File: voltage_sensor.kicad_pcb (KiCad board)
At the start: 2 copper layers, 41.6 x 56.6 mm, 24 parts, among them K1 REF, P1 Input, P2 CONN_4, P3 CONN_2, U1 REF5020, U2 LT6011, U3 ADUM5401, U4 MCP3550

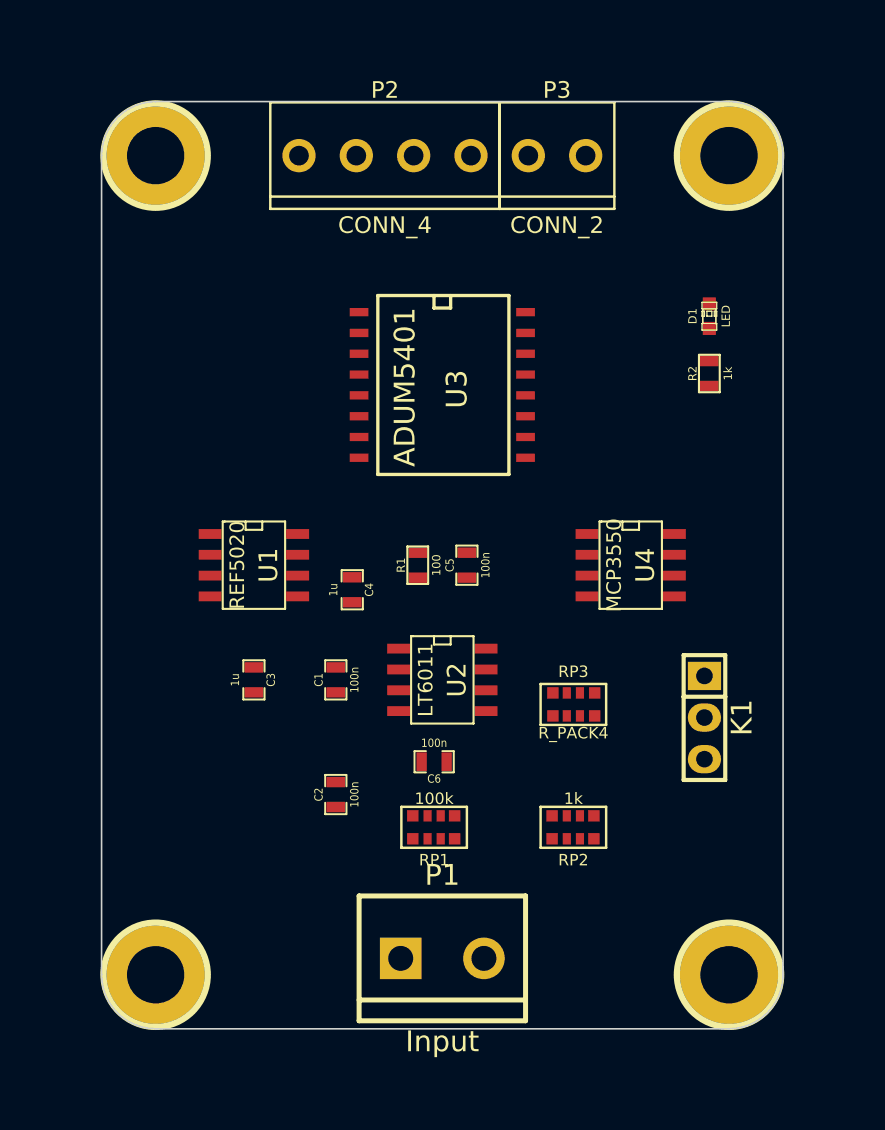
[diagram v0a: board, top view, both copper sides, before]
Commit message: Added filter caps
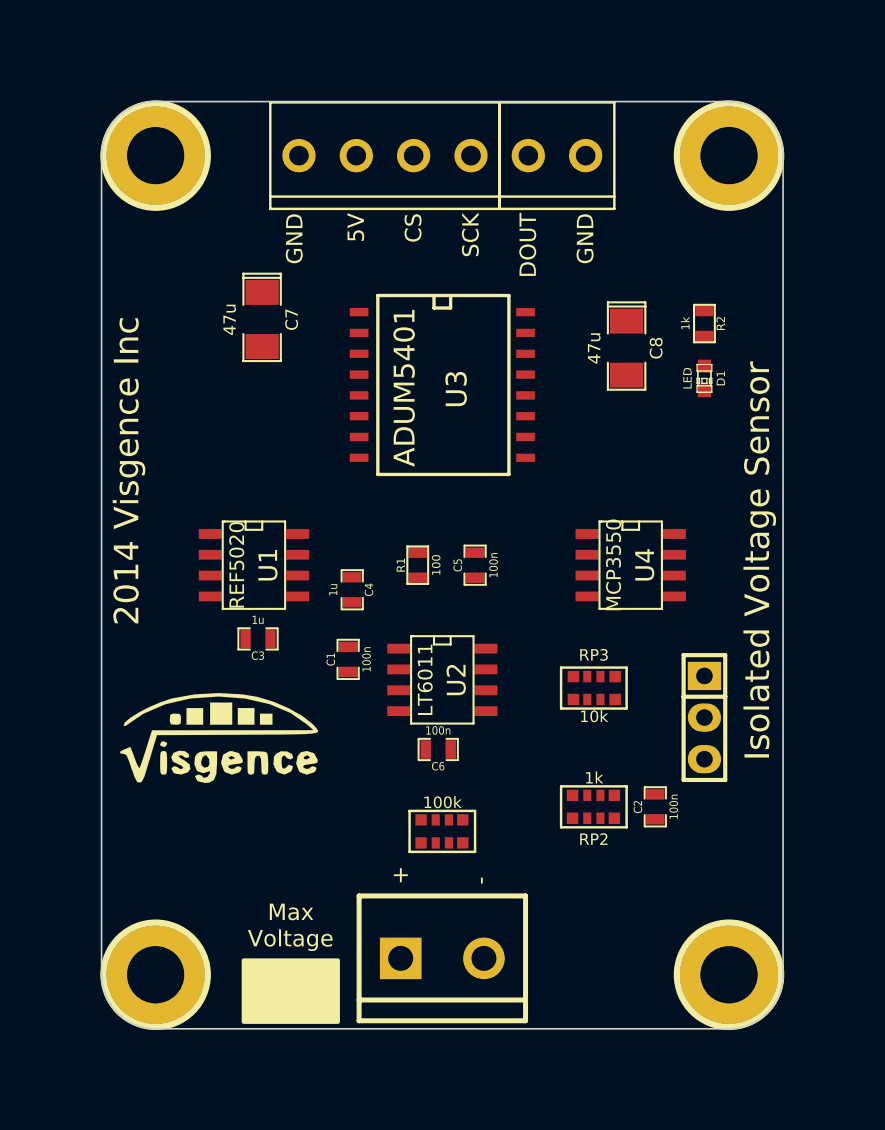
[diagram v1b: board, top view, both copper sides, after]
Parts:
- added C7: 47u, visgence_parts:SM1206POL_VIS, F.Cu at (56.5, 60.0)
- added C8: 47u, visgence_parts:SM1206POL_VIS, F.Cu at (78.8, 61.8)
- added G***: LOGO, visgence_parts:LOGOMIRROR, B.Cu at (67.5, 75.8)
- added G1: LOGO, visgence_parts:LOGO, F.Cu at (54.0, 85.5)
- RP3: value R_PACK4 -> 10k
- moved C2 19.5 mm to (80.5, 89.8)
- moved D1 3.81 mm to (83.5, 63.6), turned to 270 degrees
- moved R2 3.06 mm to (83.5, 60.2), turned to 270 degrees
- moved C3 2.51 mm to (56.2, 79.5), turned to 180 degrees
- moved RP2 1.77 mm to (76.8, 89.8)
- moved RP3 1.60 mm to (76.8, 82.5)
- moved C1 1.46 mm to (61.8, 80.8)
- moved C6 0.79 mm to (67.2, 86.2)
- moved RP1 0.56 mm to (67.5, 91.2)
- moved C5 0.50 mm to (69.5, 75.0)
- gave numbers to parts that had none: 4
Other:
- net class Default: trace_width 0.254 -> 0.4572
- board text added: "+"
- board text added: "-"
- board text added: "2014 Visgence Inc"
- board text added: "5V"
- board text added: "CS"
- board text added: "DOUT"
- board text added: "GND"
- board text added: "Isolated Voltage Sensor"
- board text added: "Max Voltage"
- board text added: "SCK"

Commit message: Routed board
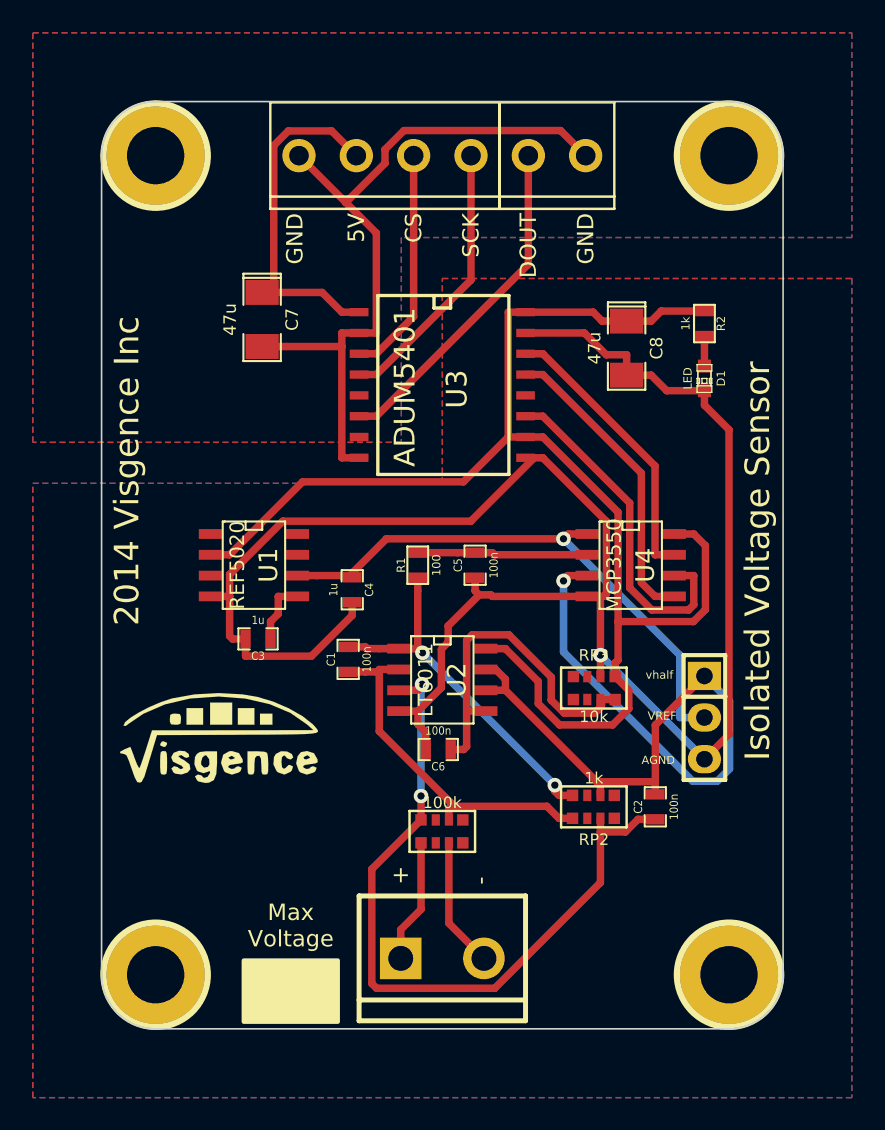
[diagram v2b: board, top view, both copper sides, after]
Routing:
- net GND: track 0.00 -> 120.0 mm, vias 0 -> 1
- net +5V: track 0.00 -> 85.8 mm
- net /vhalf: track 0.00 -> 50.0 mm, vias 0 -> 1
- net GNDIN: track 0.00 -> 46.0 mm
- net Net-(C2-Pad1): track 0.00 -> 45.5 mm, vias 0 -> 2
- net /Vref: track 0.00 -> 34.4 mm, vias 0 -> 1
- net Net-(C1-Pad2): track 0.00 -> 22.0 mm, vias 0 -> 2
- net Net-(C1-Pad1): track 0.00 -> 21.9 mm
- net Net-(C6-Pad1): track 0.00 -> 21.7 mm
- net VIN: track 0.00 -> 21.4 mm
- net DOUT: track 0.00 -> 21.3 mm
- net Net-(P3-Pad1): track 0.00 -> 20.8 mm
- net SCK: track 0.00 -> 18.6 mm
- net CS: track 0.00 -> 17.3 mm
- net Net-(P2-Pad4): track 0.00 -> 16.8 mm
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- added copper zone on B.Cu, net /vhalf
- added copper zone on F.Cu, net /vhalf
- added copper zone on B.Cu, net GNDIN
- added copper zone on F.Cu, net GNDIN
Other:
- net class Default: clearance 0.254 -> 0.2032
- rule trace_clearance: 0.254 -> 0.2032
- board text added: "AGND"
- board text added: "VREF"
- board text added: "vhalf"
